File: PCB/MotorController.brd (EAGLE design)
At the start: 84.9 x 43.8 mm, 69 parts, among them IC1 OPA333D, U1 MIC5235-3.3, U3 SAM3S4/2/1A_48PIN_LQFP, X1 12MHz, X2 08-JST-B8B-XH-A

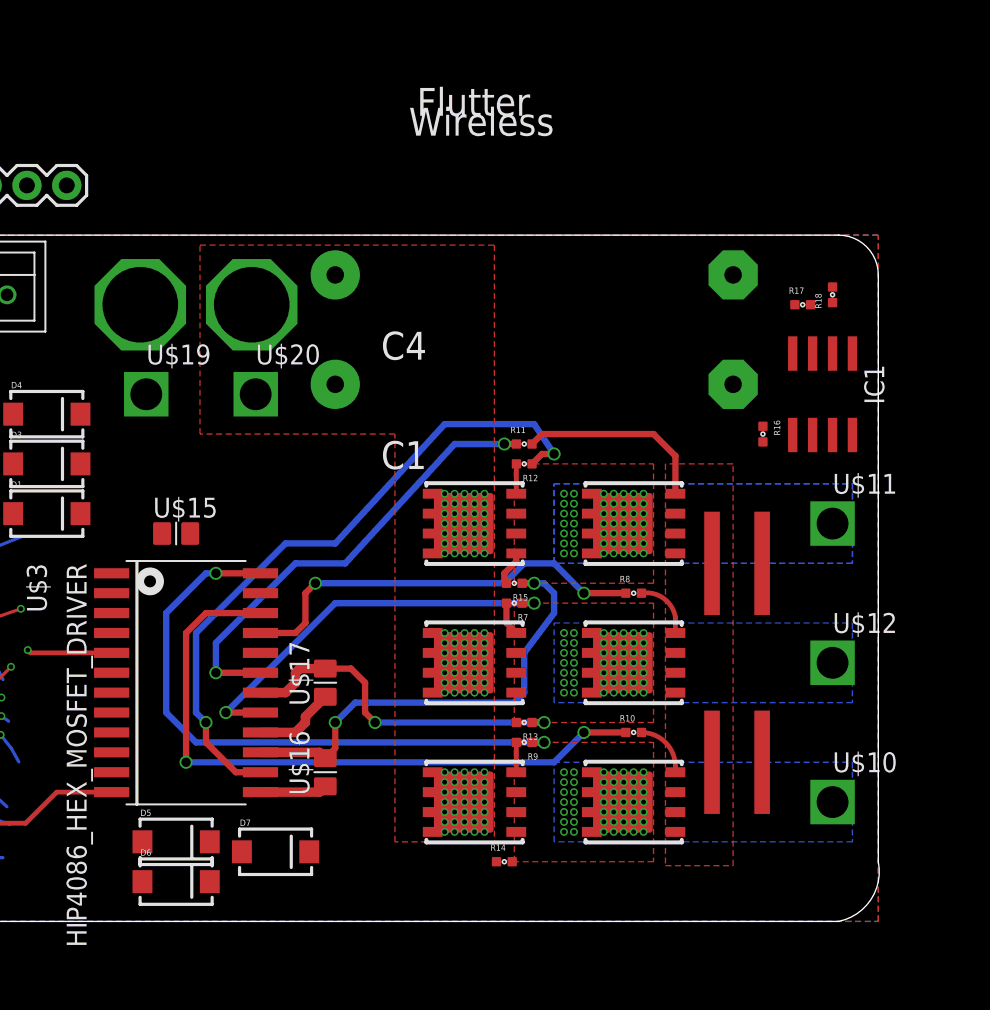
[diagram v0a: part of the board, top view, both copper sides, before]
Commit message: Move current sense circuit around, update readme
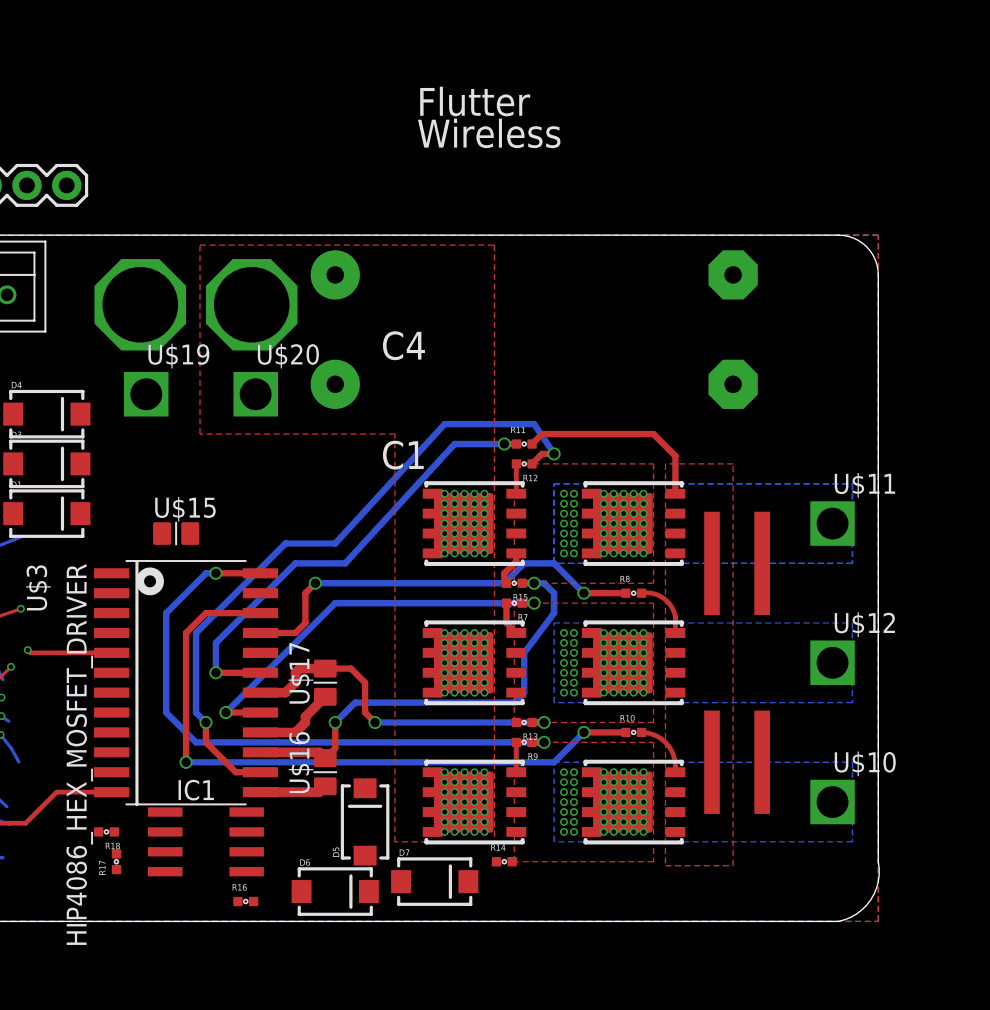
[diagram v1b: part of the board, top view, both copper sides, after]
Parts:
- moved R18 57.7 mm to (35.6, 5.71), turned to 180 degrees
- moved R17 56.4 mm to (36.2, 3.81), turned to 90 degrees
- moved IC1 48.6 mm to (41.9, 5.08), turned to 270 degrees
- moved R16 44.5 mm to (44.5, 1.27), turned to 0 degrees
- moved D5 12.1 mm to (52.1, 6.35), turned to 90 degrees
- moved D7 10.3 mm to (56.5, 2.54)
- moved D6 10.2 mm to (50.2, 1.91)
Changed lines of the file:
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@@
 <rectangle x1="-0.0254" y1="5.7912" x2="0" y2="5.8166" layer="21"/>
 <text x="55.372" y="51.435" size="1.778" layer="21" font="vector" ratio="15">Flutter</text>
-<text x="54.864" y="50.165" size="1.778" layer="21" font="vector" ratio="15">Wireless</text>
+<text x="55.372" y="49.403" size="1.778" layer="21" font="vector" ratio="15">Wireless</text>
 <text x="102.362" y="49.403" size="1.778" layer="21" font="vector" ratio="15">OSHW</text>
 <rectangle x1="32.5882" y1="10.8458" x2="38.1254" y2="10.8712" layer="30" rot="R90"/>
@@
 <element name="D3" library="SparkFun" package="SMA-DIODE" value="" x="31.75" y="29.21"/>
 <element name="D4" library="SparkFun" package="SMA-DIODE" value="" x="31.75" y="32.385"/>
-<element name="D5" library="SparkFun" package="SMA-DIODE" value="" x="40.005" y="5.08"/>
-<element name="D6" library="SparkFun" package="SMA-DIODE" value="" x="40.005" y="2.54"/>
-<element name="D7" library="SparkFun" package="SMA-DIODE" value="" x="46.355" y="4.445"/>
+<element name="D5" library="SparkFun" package="SMA-DIODE" value="" x="52.07" y="6.35" rot="R90"/>
+<element name="D6" library="SparkFun" package="SMA-DIODE" value="" x="50.165" y="1.905"/>
+<element name="D7" library="SparkFun" package="SMA-DIODE" value="" x="56.515" y="2.54"/>
 <element name="U$19" library="Taylor" package="HIGH_CURRENT_PAD2" value="HIGHCURRENTPAD2" x="38.1" y="33.655"/>
 <element name="U$20" library="Taylor" package="HIGH_CURRENT_PAD2" value="HIGHCURRENTPAD2" x="45.085" y="33.655"/>
@@
 <element name="R15" library="Taylor" package="0402-RES" value="4.7" x="61.595" y="21.59" rot="R180"/>
 <element name="LED1" library="adafruit" package="WS2812" value="WS2812" x="6.35" y="30.48"/>
-<element name="IC1" library="linear" package="SO08" value="OPA333D" x="81.28" y="33.655" rot="R180"/>
-<element name="R16" library="Taylor" package="0402-RES" value="4.7" x="77.47" y="31.115" rot="R270"/>
-<element name="R17" library="Taylor" package="0402-RES" value="4.7" x="80.01" y="39.37"/>
-<element name="R18" library="Taylor" package="0402-RES" value="4.7" x="81.915" y="40.005" rot="R90"/>
+<element name="IC1" library="linear" package="SO08" value="OPA333D" x="41.91" y="5.08" rot="R270"/>
+<element name="R16" library="Taylor" package="0402-RES" value="4.7" x="44.45" y="1.27"/>
+<element name="R17" library="Taylor" package="0402-RES" value="4.7" x="36.195" y="3.81" rot="R90"/>
+<element name="R18" library="Taylor" package="0402-RES" value="4.7" x="35.56" y="5.715" rot="R180"/>
 <element name="JP1" library="SparkFun" package="1X10" value="M10&quot;" x="10.16" y="46.99"/>
 <element name="U$21" library="Taylor" package="XT60_CONNECTOR" value="XT60" x="41.275" y="39.37" rot="R90"/>
@@
 <contactref element="IC1" pad="6"/>
 <contactref element="R16" pad="2"/>
-<wire x1="80.645" y1="31.055" x2="79.51" y2="39.37" width="0" layer="19" extent="1-1"/>
-<wire x1="77.47" y1="30.615" x2="80.645" y2="31.055" width="0" layer="19" extent="1-1"/>
-<wire x1="24.4" y1="6.67" x2="77.47" y2="30.615" width="0" layer="19" extent="1-1"/>
+<wire x1="44.95" y1="1.27" x2="44.51" y2="4.445" width="0" layer="19" extent="1-1"/>
+<wire x1="36.195" y1="3.31" x2="44.51" y2="4.445" width="0" layer="19" extent="1-1"/>
+<wire x1="24.4" y1="4.08" x2="36.195" y2="3.31" width="0" layer="19" extent="1-2"/>
 </signal>
 <signal name="A3/PWML0">
@@
 </polygon>
 <contactref element="IC1" pad="3"/>
-<wire x1="71.882" y1="26.035" x2="80.645" y2="36.255" width="0" layer="19" extent="1-1"/>
+<wire x1="71.882" y1="5.715" x2="39.31" y2="4.445" width="0" layer="19" extent="1-1"/>
 </signal>
 <signal name="CLO">
@@
 <wire x1="49.53" y1="10.425" x2="49.16" y2="10.795" width="0.6096" layer="1"/>
 <wire x1="49.16" y1="10.795" x2="45.39" y2="10.795" width="0.6096" layer="1"/>
-<wire x1="42.155" y1="5.08" x2="45.39" y2="10.795" width="0" layer="19" extent="1-1"/>
+<wire x1="50.165" y1="11.06" x2="52.07" y2="8.5" width="0" layer="19" extent="1-1"/>
 </signal>
 <signal name="BHS">
@@
 <contactref element="D7" pad="C"/>
 <wire x1="40.905" y1="24.765" x2="45.39" y2="20.955" width="0" layer="19" extent="1-1"/>
-<wire x1="48.505" y1="4.445" x2="45.39" y2="20.955" width="0" layer="19" extent="1-1"/>
-<wire x1="60.46" y1="3.81" x2="48.505" y2="4.445" width="0" layer="19" extent="1-1"/>
+<wire x1="58.665" y1="2.54" x2="45.39" y2="20.955" width="0" layer="19" extent="1-1"/>
+<wire x1="60.46" y1="3.81" x2="58.665" y2="2.54" width="0" layer="19" extent="1-1"/>
 </signal>
 <signal name="AHS">
@@
 <wire x1="47.625" y1="15.24" x2="46.99" y2="14.605" width="0.6096" layer="1"/>
 <wire x1="46.99" y1="14.605" x2="45.39" y2="14.605" width="0.6096" layer="1"/>
-<wire x1="42.155" y1="2.54" x2="45.39" y2="14.605" width="0" layer="19" extent="1-1"/>
+<wire x1="52.315" y1="1.905" x2="52.705" y2="12.7" width="0" layer="19" extent="1-16"/>
 </signal>
 <signal name="N$1">
@@
 <contactref element="LED1" pad="VDD"/>
 <contactref element="LED1" pad="LEDVDD"/>
-<wire x1="8.35" y1="32.18" x2="81.915" y2="31.055" width="0" layer="19" extent="1-1"/>
+<wire x1="8.35" y1="32.18" x2="44.51" y2="5.715" width="0" layer="19" extent="1-1"/>
 <wire x1="4.35" y1="30.48" x2="8.35" y2="32.18" width="0" layer="19" extent="1-1"/>
 </signal>
@@
 <contactref element="R18" pad="1"/>
 <contactref element="R17" pad="2"/>
-<wire x1="80.51" y1="39.37" x2="81.915" y2="39.505" width="0" layer="19" extent="1-1"/>
-<wire x1="81.915" y1="36.255" x2="81.915" y2="39.505" width="0" layer="19" extent="1-1"/>
+<wire x1="36.06" y1="5.715" x2="39.31" y2="5.715" width="0" layer="19" extent="1-1"/>
+<wire x1="36.195" y1="4.31" x2="36.06" y2="5.715" width="0" layer="19" extent="1-1"/>
 </signal>
 <signal name="N$3">
